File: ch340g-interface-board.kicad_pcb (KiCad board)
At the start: 2 copper layers, 37.2 x 19.2 mm, 10 parts, among them J1 61729-1011BLF, J2 Conn_01x02_Pin, J3 Conn_01x06_Pin, U1 CH340G, Y1 12Mhz

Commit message: documentation: board updates
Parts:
- J3: value Conn_01x06_Pin -> Conn_01x07_Pin; footprint Connector_PinHeader_1.00mm:PinHeader_1x06_P1.00mm_Vertical -> Connector_PinHeader_1.00mm:PinHeader_1x07_P1.00mm_Vertical
- moved J2 9.76 mm to (105.2, 84.6)
- moved J3 4.35 mm to (105.2, 75.1)
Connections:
- J3 pad 1: Net-(J3-Pin_1) -> GND
- U1 pad 10: Net-(J3-Pin_5) -> Net-(J3-Pin_6)
- U1 pad 11: Net-(J3-Pin_4) -> Net-(J3-Pin_5)
- U1 pad 12: Net-(J3-Pin_3) -> Net-(J3-Pin_4)
- U1 pad 13: Net-(J3-Pin_2) -> Net-(J3-Pin_3)
- U1 pad 14: Net-(J3-Pin_1) -> Net-(J3-Pin_2)
- U1 pad 9: Net-(J3-Pin_6) -> Net-(J3-Pin_7)
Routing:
- net Net-(J3-Pin_7): track 0.00 -> 6.31 mm
- net Net-(J3-Pin_1): track 3.52 -> 0.00 mm
- net Net-(U1-XO): track 31.5 -> 35.0 mm
- net Net-(U1-XI): track 20.9 -> 23.5 mm
- net Net-(J3-Pin_6): track 4.08 -> 6.69 mm
- net Net-(J3-Pin_5): track 3.97 -> 6.25 mm
- net Net-(J3-Pin_4): track 3.86 -> 6.09 mm
- net Net-(J3-Pin_3): track 3.74 -> 5.61 mm
- net Net-(J3-Pin_2): track 3.63 -> 5.10 mm
- net Net-(J2-Pin_1): track 10.4 -> 11.3 mm, vias 0 -> 1
- net Net-(J2-Pin_2): track 10.2 -> 10.6 mm, vias 0 -> 1

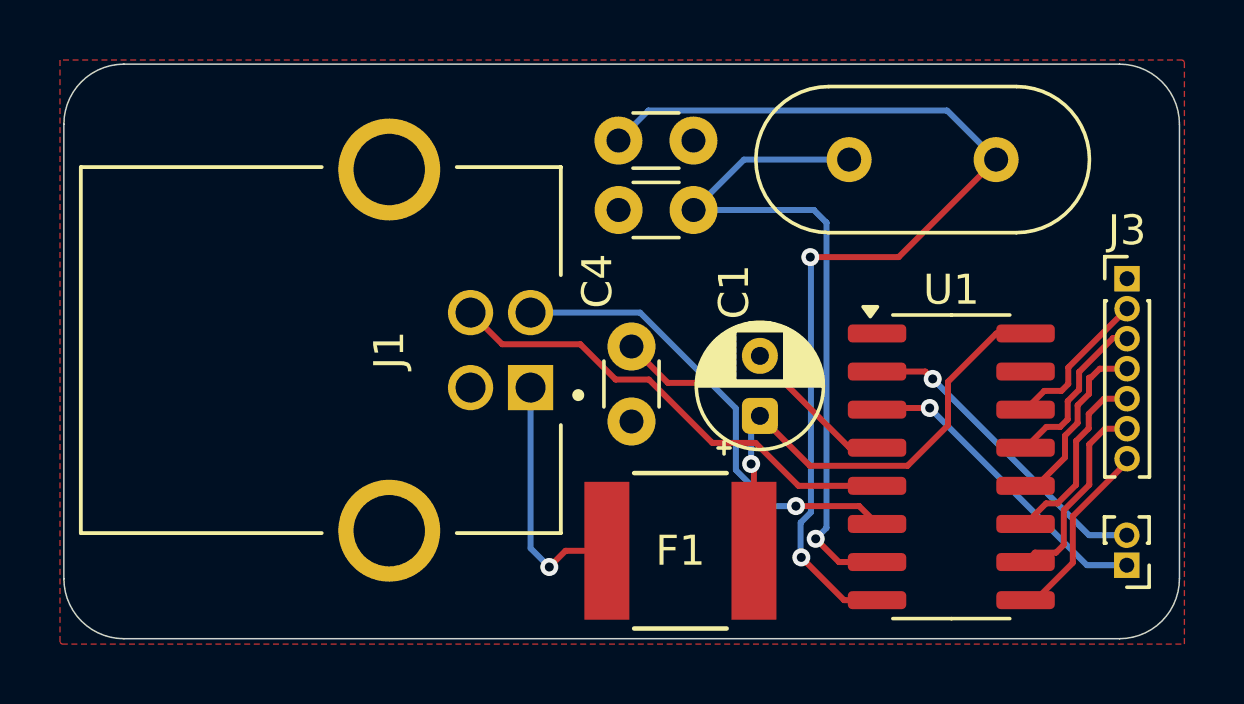
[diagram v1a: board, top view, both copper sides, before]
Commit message: documentation: board updates
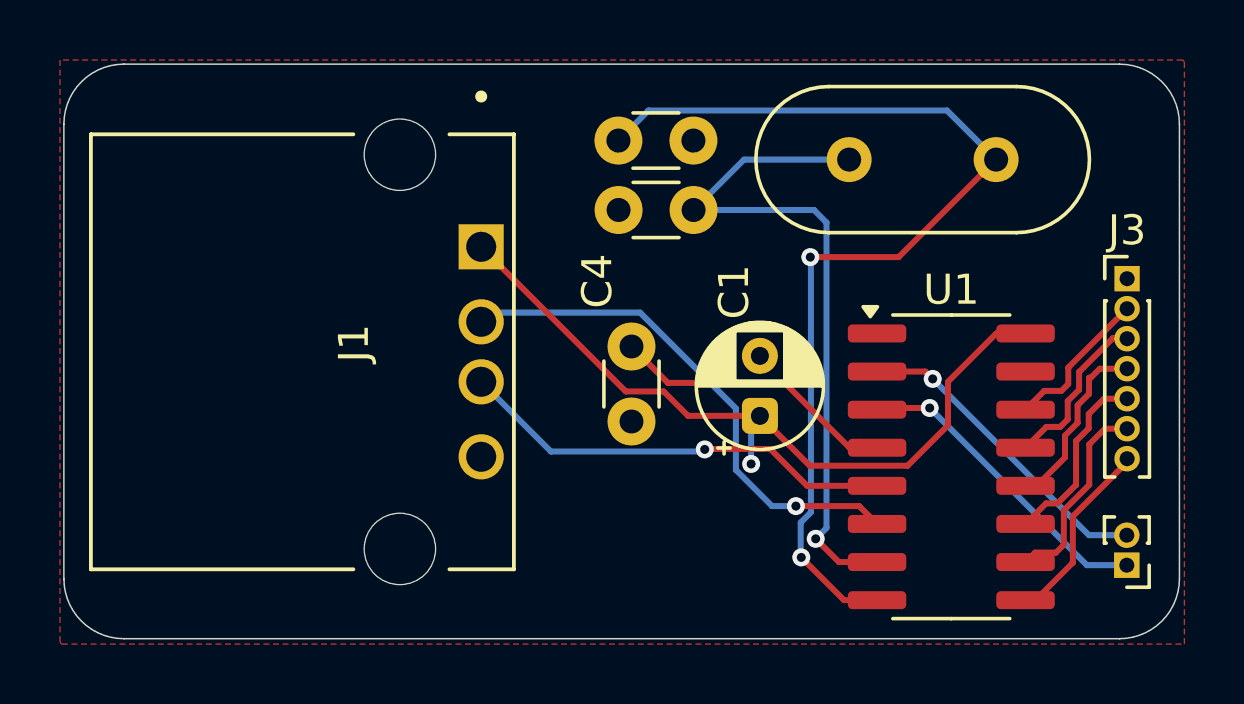
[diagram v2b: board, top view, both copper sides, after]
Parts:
- removed F1: MF-SMDF050-2, FUSE_SMDF050-2:FUSE_SMDF050-2
- J1: value 61729-1011BLF -> USB-A1HSW6; footprint 61729-1011BLF:AMPHENOL_61729-1011BLF -> USB-A1HSW6:OST_USB-A1HSW6
- moved J1 0.36 mm to (81.0, 77.5)
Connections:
- J1 pad 1: Net-(J1-VCC) -> +5V
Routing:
- net +5V: track 16.9 -> 25.7 mm
- net Net-(J1-VCC): track 8.38 -> 0.00 mm, vias 1 -> 0
- net /D-: track 15.7 -> 17.4 mm
- net /D+: track 15.9 -> 14.7 mm, vias 0 -> 1
